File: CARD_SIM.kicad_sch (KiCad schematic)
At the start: 4 parts, among them J1 MSIM-11-C

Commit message: added 3.3v gpio input protection
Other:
- moved on the sheet: C53, C54, J1, R47

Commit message: finished initial esp routing
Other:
- moved on the sheet: R47
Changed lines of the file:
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@@
 	(generator_version "9.0")
 	(paper "A5")
-	(rectangle
-		(start 55.88 35.56)
-		(end 127 83.82)
-		(stroke
-			(width 0)
-			(type default)
-		)
-		(fill
-			(type none)
-		)
-	)
 	(text_box "Mini SIM\nCellular"
 		(exclude_from_sim no)
-		(at 55.88 36.83 0)
+		(at 90.17 104.14 0)
 		(size 30.48 6.35)
 		(margins 0.9525 0.9525 0.9525 0.9525)
@@
 	)
 	(junction
+		(at 64.77 55.88)
+		(diameter 0)
+		(color 0 0 0 0)
+	)
+	(junction
 		(at 124.46 55.88)
 		(diameter 0)
 		(color 0 0 0 0)
 	)
-	(junction
-		(at 86.36 55.88)
-		(diameter 0)
-		(color 0 0 0 0)
-	)
 	(no_connect
 		(at 96.52 58.42)
@@
 	(wire
 		(pts
-			(xy 86.36 55.88) (xy 96.52 55.88)
-		)
-		(stroke
-			(width 0)
-			(type default)
-		)
-	)
-	(wire
-		(pts
-			(xy 86.36 44.45) (xy 86.36 45.72)
+			(xy 64.77 44.45) (xy 64.77 45.72)
 		)
 		(stroke
@@
 	(wire
 		(pts
-			(xy 76.2 55.88) (xy 64.77 55.88)
-		)
-		(stroke
-			(width 0)
-			(type default)
-		)
-	)
-	(wire
-		(pts
 			(xy 64.77 55.88) (xy 64.77 57.15)
 		)
@@
 	(wire
 		(pts
-			(xy 86.36 53.34) (xy 86.36 55.88)
+			(xy 64.77 53.34) (xy 64.77 55.88)
 		)
 		(stroke
@@
 	(wire
 		(pts
-			(xy 76.2 55.88) (xy 86.36 55.88)
-		)
-		(stroke
-			(width 0)
-			(type default)
-		)
-	)
-	(wire
-		(pts
 			(xy 90.17 63.5) (xy 96.52 63.5)
 		)
@@
 	(wire
 		(pts
+			(xy 64.77 55.88) (xy 76.2 55.88)
+		)
+		(stroke
+			(width 0)
+			(type default)
+		)
+	)
+	(wire
+		(pts
 			(xy 64.77 67.31) (xy 64.77 64.77)
+		)
+		(stroke
+			(width 0)
+			(type default)
+		)
+	)
+	(wire
+		(pts
+			(xy 76.2 55.88) (xy 96.52 55.88)
 		)
 		(stroke
@@
 		(on_board yes)
 		(dnp no)
-		(property "Reference" "#PWR0100"
+		(property "Reference" "#PWR0298"
 			(at 26.67 27.94 0)
 			(effects
@@
 			(project "NCU"
 				(path "/3aee14c3-5480-4f7c-989e-3fef81779034/9e564c38-7205-44f8-b5f6-41c7c4a47ab0"
-					(reference "#PWR0100")
+					(reference "#PWR0298")
 					(unit 1)
 				)
@@
 	(symbol
 		(lib_id "Device:R")
-		(at 86.36 49.53 0)
+		(at 64.77 49.53 0)
 		(mirror x)
 		(unit 1)
@@
 		(dnp no)
 		(property "Reference" "R47"
-			(at 89.662 48.768 0)
+			(at 68.072 48.768 0)
 			(effects
 				(font
@@
 		)
 		(property "Value" "10R"
-			(at 89.662 50.546 0)
+			(at 68.072 50.546 0)
 			(effects
 				(font
@@
 		)
 		(property "Footprint" "Resistor_SMD:R_0603_1608Metric_Pad0.98x0.95mm_HandSolder"
-			(at 84.582 49.53 90)
+			(at 62.992 49.53 90)
 			(effects
 				(font
@@
 		)
 		(property "Datasheet" "~"
-			(at 86.36 49.53 0)
+			(at 64.77 49.53 0)
 			(effects
 				(font
@@
 		)
 		(property "Description" "Resistor"
-			(at 86.36 49.53 0)
+			(at 64.77 49.53 0)
 			(effects
 				(font
@@
 		(on_board yes)
 		(dnp no)
-		(property "Reference" "#PWR099"
+		(property "Reference" "#PWR0299"
 			(at 26.67 35.56 0)
 			(effects
@@
 			(project "NCU"
 				(path "/3aee14c3-5480-4f7c-989e-3fef81779034/9e564c38-7205-44f8-b5f6-41c7c4a47ab0"
-					(reference "#PWR099")
+					(reference "#PWR0299")
 					(unit 1)
 				)
@@
 	(symbol
 		(lib_id "power:+5V")
-		(at 86.36 44.45 0)
+		(at 64.77 44.45 0)
 		(mirror y)
 		(unit 1)
@@
 		(dnp no)
 		(property "Reference" "#PWR089"
-			(at 86.36 48.26 0)
+			(at 64.77 48.26 0)
 			(effects
 				(font
@@
 		)
 		(property "Value" "+3V3"
-			(at 86.614 40.386 0)
+			(at 65.024 40.386 0)
 			(effects
 				(font
@@
 		)
 		(property "Footprint" ""
-			(at 86.36 44.45 0)
+			(at 64.77 44.45 0)
 			(effects
 				(font
@@
 		)
 		(property "Datasheet" ""
-			(at 86.36 44.45 0)
+			(at 64.77 44.45 0)
 			(effects
 				(font
@@
 		)
 		(property "Description" "Power symbol creates a global label with name \"+5V\""
-			(at 86.36 44.45 0)
-			(effects
-				(font
+			(at 64.77 44.45 0)
+			(effects
+				(font

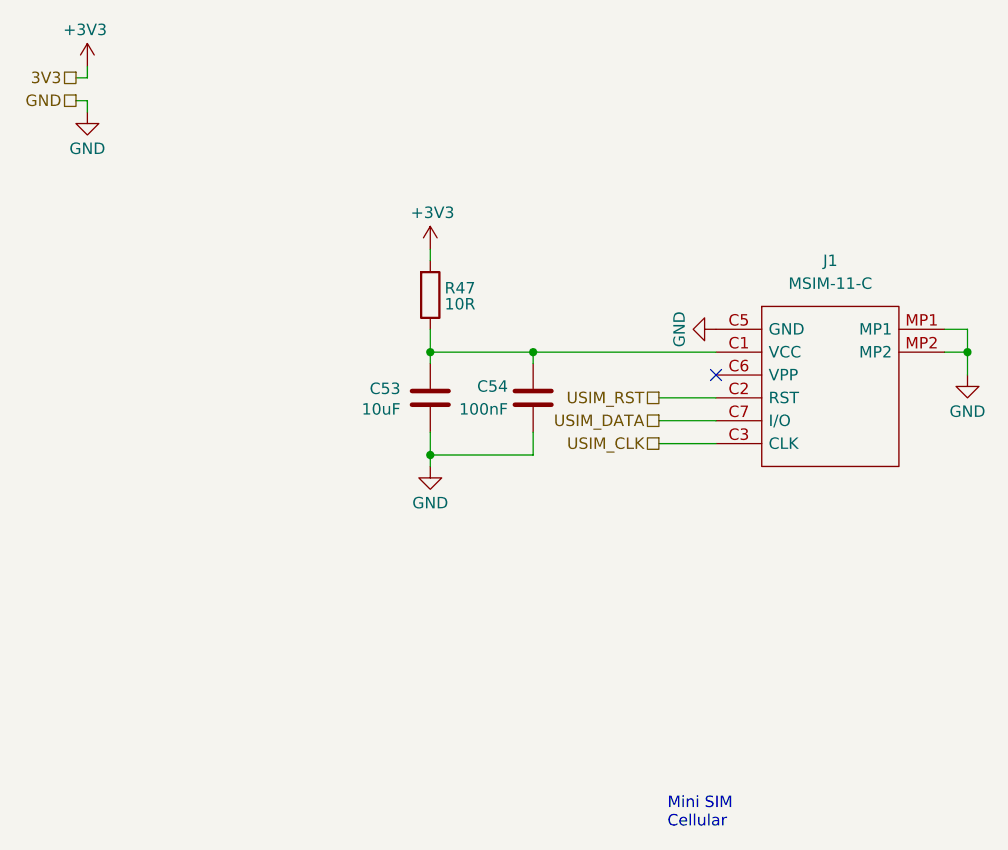
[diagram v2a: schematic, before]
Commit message: added dip switches to wireless disables
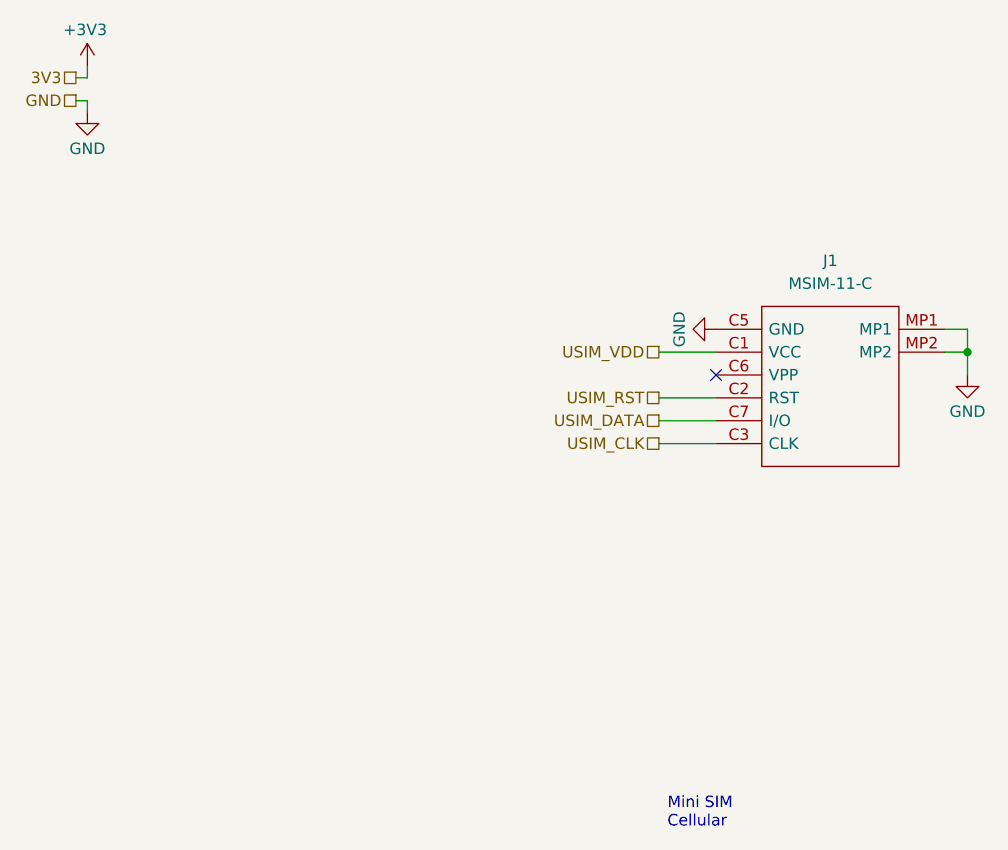
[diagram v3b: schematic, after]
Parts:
- removed C53: 10uF, Capacitor_SMD:C_0603_1608Metric_Pad1.08x0.95mm_HandSolder, symbol Device:C
- removed C54: 100nF, Capacitor_SMD:C_0603_1608Metric_Pad1.08x0.95mm_HandSolder, symbol Device:C
- removed R47: 10R, Resistor_SMD:R_0603_1608Metric_Pad0.98x0.95mm_HandSolder, symbol Device:R
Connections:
- net USIM_VDD: now reaches J1.C1 (VCC)

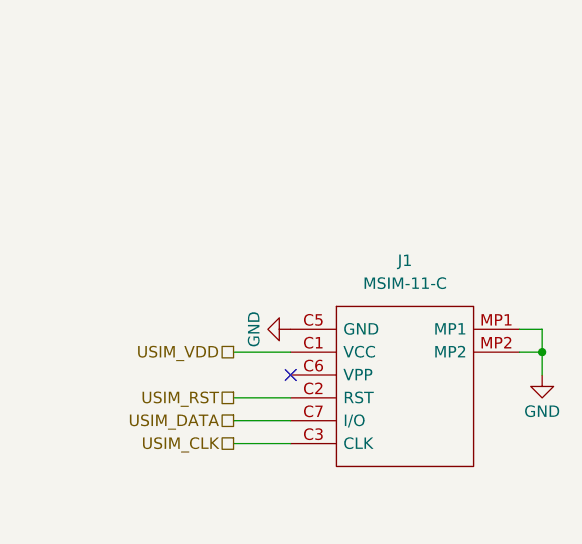
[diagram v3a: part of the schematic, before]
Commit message: redid annotations, added test point
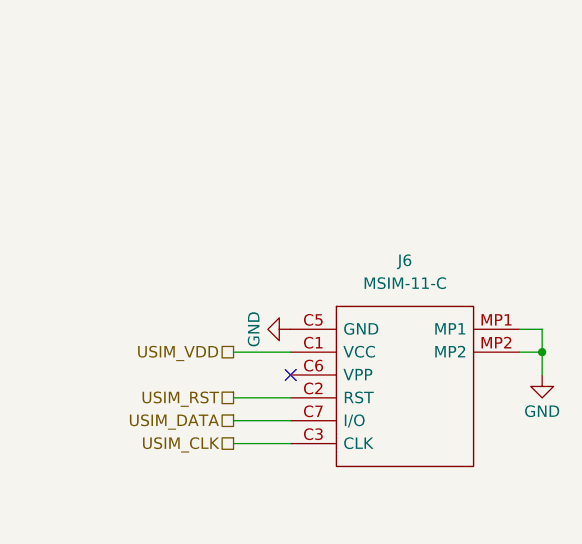
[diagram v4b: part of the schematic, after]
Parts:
- renumbered J1 to J6
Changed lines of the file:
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@@
 		(dnp no)
 		(fields_autoplaced yes)
-		(property "Reference" "J1"
+		(property "Reference" "J6"
 			(at 109.22 45.72 0)
 			(effects
@@
 			(project "NCU"
 				(path "/3aee14c3-5480-4f7c-989e-3fef81779034/9e564c38-7205-44f8-b5f6-41c7c4a47ab0"
-					(reference "J1")
+					(reference "J6")
 					(unit 1)
 				)
@@
 		(on_board yes)
 		(dnp no)
-		(property "Reference" "#PWR042"
+		(property "Reference" "#PWR0197"
 			(at 90.17 53.34 0)
 			(effects
@@
 			(project "NCU"
 				(path "/3aee14c3-5480-4f7c-989e-3fef81779034/9e564c38-7205-44f8-b5f6-41c7c4a47ab0"
-					(reference "#PWR042")
+					(reference "#PWR0197")
 					(unit 1)
 				)
@@
 		(on_board yes)
 		(dnp no)
-		(property "Reference" "#PWR028"
+		(property "Reference" "#PWR0199"
 			(at 124.46 64.77 0)
 			(effects
@@
 			(project "NCU"
 				(path "/3aee14c3-5480-4f7c-989e-3fef81779034/9e564c38-7205-44f8-b5f6-41c7c4a47ab0"
-					(reference "#PWR028")
+					(reference "#PWR0199")
 					(unit 1)
 				)
@@
 		(on_board yes)
 		(dnp no)
-		(property "Reference" "#PWR0298"
+		(property "Reference" "#PWR0193"
 			(at 26.67 27.94 0)
 			(effects
@@
 			(project "NCU"
 				(path "/3aee14c3-5480-4f7c-989e-3fef81779034/9e564c38-7205-44f8-b5f6-41c7c4a47ab0"
-					(reference "#PWR0298")
+					(reference "#PWR0193")
 					(unit 1)
 				)
@@
 		(on_board yes)
 		(dnp no)
-		(property "Reference" "#PWR0299"
+		(property "Reference" "#PWR0194"
 			(at 26.67 35.56 0)
 			(effects
@@
 			(project "NCU"
 				(path "/3aee14c3-5480-4f7c-989e-3fef81779034/9e564c38-7205-44f8-b5f6-41c7c4a47ab0"
-					(reference "#PWR0299")
-					(unit 1)
-				)
+					(reference "#PWR0194")
+					(unit 1)
+				)
